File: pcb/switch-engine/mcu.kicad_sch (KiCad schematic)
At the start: 67 parts, among them J10 CORTEX_DEBUG_ETM, J11 CONN_01X03, J12 CONN_01X03, J13 PMOD_HOST, J9 PMOD_HOST, U14 ECS-1612MV-250-CN, U16 ECS-1612MV-250-CN, U17 AT24MAC402, U8 XILINX_ULTRASCALEPLUS_B676, U9 STM32H735-UFBGA176-25

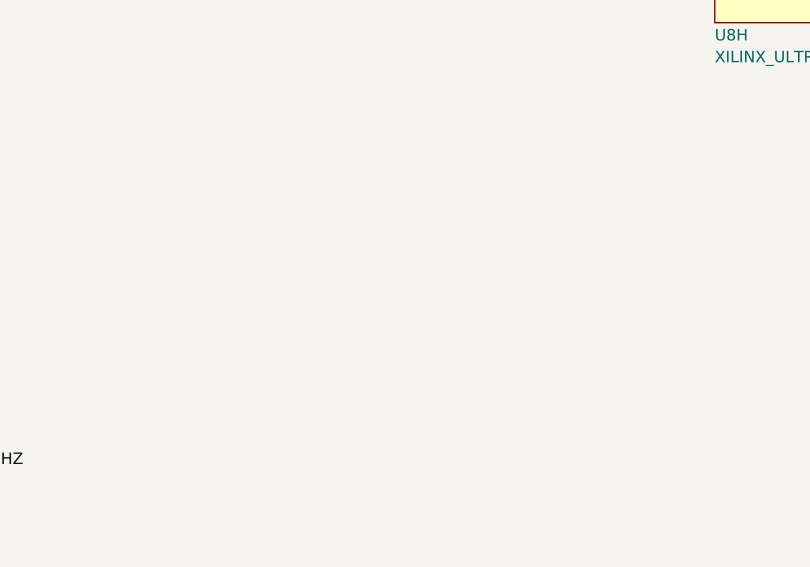
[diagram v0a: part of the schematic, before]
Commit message: Continued initial schematic work on switch engine
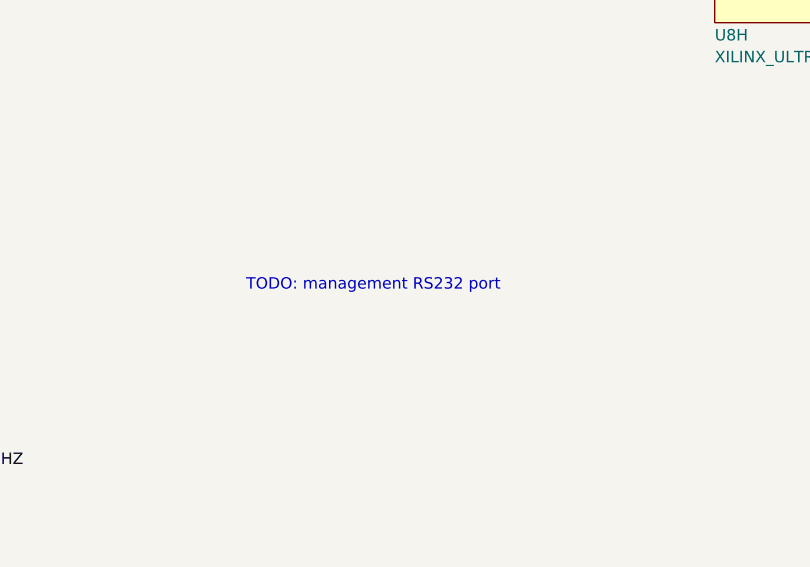
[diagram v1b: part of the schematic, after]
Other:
- note added: "TODO: management RS232 port"
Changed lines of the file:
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@@
+		)
+	)
+	(text "TODO: management RS232 port"
+		(exclude_from_sim no)
+		(at 295.91 214.63 0)
+		(effects
+			(font
+				(size 1.27 1.27)
+			)
+			(justify left)
 		)
 	)

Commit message: First iteration of main board PCB schematic is now passing ERC
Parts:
- removed C102: 0.47 uF, azonenberg_pcb:EIA_0402_CAP_NOSILK, symbol device:C
- removed J11: CONN_01X03, azonenberg_pcb:CONN_HEADER_2.54MM_1x3, symbol conn:CONN_01X03
- removed R71: 33, azonenberg_pcb:EIA_0402_RES_NOSILK, symbol device:R
- removed U16: ECS-1612MV-250-CN, azonenberg_pcb:OSCILLATOR_1.6x1.2, symbol osc-azonenberg:OSC
- added C149: 0.47 uF, azonenberg_pcb:EIA_0402_CAP_NOSILK, symbol device:C
- added C150, C151, C152, C153: 0.1 uF, azonenberg_pcb:EIA_0402_CAP_NOSILK, symbol device:C
- added J24, J25: JUMPER_0402_SPDT, azonenberg_pcb:EIA_0402_JUMPER, symbol special-azonenberg:JUMPER_0402_SPDT
- added J26: RJ45, azonenberg_pcb:CONN_RJ45_BELSTEWART_SS-7188S-A-PG4-1-BA-xx, symbol conn:RJ45
- added TP25, TP26, TP27, TP28: CONN_01X03, azonenberg_pcb:CONN_HEADER_2.54MM_1x3, symbol conn:CONN_01X03
- added U29: ADM3101E_QFN, azonenberg_pcb:QFN_12_0.5MM_3x3MM, symbol special-azonenberg:ADM3101E_QFN
- U8: value XILINX_ULTRASCALEPLUS_B676 -> XCKU5P-2FFVB676I
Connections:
- net FPGA_CLK_25MHZ is gone; now on net FMC_AD4: U8.E13 (IO_L7P_HDGC_87)
- net 3V3: now also C149.1, U29.5 (VCC)
- net GND: now also C149.2, C151.2, C153.2, J26.4, J26.5, J26.9 (SHIELD), TP25.3 (P3), TP26.3 (P3), TP27.3 (P3), TP28.3 (P3), U29.6 (GND), U29.PAD (GND)
- net MCU_UART_RX: now also TP28.1 (P1), U29.2 (Rout)
- net MCU_UART_TX: now also TP28.2 (P2), U29.3 (Tin)
- net MGMT_I2C_SCL: now also TP25.2 (P2)
- net MGMT_I2C_SDA: now also TP25.1 (P1)
- net SFP0_SCL: now also TP26.2 (P2)
- net SFP0_SDA: now also TP26.1 (P1)
- net SFP1_SCL: now also TP27.2 (P2)
- net SFP1_SDA: now also TP27.1 (P1)
- net FAN2_PWM: now reaches U9.N5 (PA3)
- net FAN1_TACH: now reaches U9.P1 (PA0)
- net FAN2_TACH: now reaches U9.P2 (PA1)
- net FAN1_PWM: now reaches U9.R2 (PA2)
- new net: C150.1, U29.11 (C2+)
- new net: C150.2, U29.10 (C2-)
- new net: C153.1, U29.4 (V+)
- new net: C152.1, U29.1 (C1+)
- new net: C152.2, U29.12 (C1-)
- new net: C151.1, U29.7 (V-)
- new net RS232_RX: J24.3, J25.1, U29.9 (Rin)
- new net RS232_RX_RJ45: J25.2, J26.6
- new net RS232_TX: J24.1, J25.3, U29.8 (Tout)
- new net RS232_TX_RJ45: J24.2, J26.3
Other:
- note added: "Clocks"
- note added: "FPGA GPIO"
- note added: "FPGA IOs to MCU"
- note added: "MAC EEPROM"
- note added: "MCU GPIO"
- note added: "MCU IO banks"
- note added: "MCU power/debug"
- note added: "RS232 console"
- note added: "TX/RX crossover jumpers in case we got the RJ45 pinout wrong :)"
- note added: "Test points"
- note removed: "TODO: management RS232 port"
- company: (none) -> Antikernel Labs
- title: (none) -> LATENTRED Ethernet Switch - Main Board
- moved on the sheet: C100, C101, C103, C72, C73, C74, C75, C76, C77, C78, C79, C80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

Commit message: Finished schematic review
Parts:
- removed J24, J25: JUMPER_0402_SPDT, azonenberg_pcb:EIA_0402_JUMPER, symbol special-azonenberg:JUMPER_0402_SPDT
- added R71, R9: 0, symbol device:R
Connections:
- net RS232_RX: now also R71.1
- net RS232_RX_RJ45: now also R71.2
- net RS232_TX: now also R9.1
- net RS232_TX_RJ45: now also R9.2
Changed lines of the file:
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@@
 	(text "TX/RX crossover jumpers\nin case we got the RJ45 pinout wrong :)"
 		(exclude_from_sim no)
-		(at 314.96 193.04 0)
+		(at 307.34 179.07 0)
 		(effects
 			(font
@@
 	)
 	(label "RS232_RX_RJ45"
-		(at 307.34 182.88 180)
+		(at 314.96 172.72 0)
 		(fields_autoplaced yes)
 		(effects
@@
 				(size 1.27 1.27)
 			)
-			(justify right bottom)
+			(justify left bottom)
 		)
 	)
@@
 		)
 	)
-	(label "RS232_TX"
-		(at 307.34 185.42 180)
-		(fields_autoplaced yes)
-		(effects
-			(font
-				(size 1.27 1.27)
-			)
-			(justify right bottom)
-		)
-	)
 	(label "FMC_NOE"
 		(at 228.6 62.23 180)
@@
 		)
 	)
-	(label "RS232_RX"
-		(at 307.34 172.72 180)
-		(fields_autoplaced yes)
-		(effects
-			(font
-				(size 1.27 1.27)
-			)
-			(justify right bottom)
-		)
-	)
 	(label "GND"
 		(at 306.07 106.68 180)
@@
 	)
 	(label "RS232_RX"
-		(at 307.34 180.34 180)
+		(at 307.34 172.72 180)
 		(fields_autoplaced yes)
 		(effects
@@
 	)
 	(label "RS232_TX_RJ45"
-		(at 307.34 170.18 180)
+		(at 314.96 167.64 0)
 		(fields_autoplaced yes)
 		(effects
@@
 				(size 1.27 1.27)
 			)
-			(justify right bottom)
+			(justify left bottom)
 		)
 	)
@@
 	)
 	(symbol
-		(lib_id "special-azonenberg:JUMPER_0402_SPDT")
-		(at 314.96 175.26 0)
-		(mirror y)
-		(unit 1)
-		(exclude_from_sim no)
-		(in_bom yes)
-		(on_board yes)
-		(dnp no)
-		(fields_autoplaced yes)
-		(property "Reference" "J24"
-			(at 324.485 169.1153 0)
-			(effects
-				(font
-					(size 1.524 1.524)
-				)
-				(justify right)
-			)
-		)
-		(property "Value" "JUMPER_0402_SPDT"
-			(at 324.485 172.3943 0)
-			(effects
-				(font
-					(size 1.524 1.524)
-				)
-				(justify right)
-			)
-		)
-		(property "Footprint" "azonenberg_pcb:EIA_0402_JUMPER"
-			(at 314.96 175.26 0)
-			(effects
-				(font
-					(size 1.524 1.524)
-				)
-				(hide yes)
-			)
-		)
-		(property "Datasheet" ""
-			(at 314.96 175.26 0)
-			(effects
-				(font
-					(size 1.524 1.524)
-				)
-			)
-		)
-		(property "Description" ""
-			(at 314.96 175.26 0)
-			(effects
-				(font
-					(size 1.27 1.27)
-				)
-				(hide yes)
-			)
-		)
-		(pin "1"
-		)
-		(pin "2"
-		)
-		(pin "3"
-		)
-		(instances
-			(project "switch-engine"
-				(path "/2594b26d-2fe5-4054-81d2-ca5df3747243/16e4b61f-e96f-427b-b17b-02c8899758b5"
-					(reference "J24")
-					(unit 1)
-				)
-			)
-		)
-	)
-	(symbol
 		(lib_id "device:C")
 		(at 99.06 138.43 0)
@@
 	)
 	(symbol
+		(lib_id "device:R")
+		(at 311.15 172.72 90)
+		(unit 1)
+		(exclude_from_sim no)
+		(in_bom yes)
+		(on_board yes)
+		(dnp no)
+		(property "Reference" "R71"
+			(at 311.15 170.18 90)
+			(effects
+				(font
+					(size 1.27 1.27)
+				)
+			)
+		)
+		(property "Value" "0"
+			(at 311.15 172.72 90)
+			(effects
+				(font
+					(size 1.27 1.27)
+				)
+			)
+		)
+		(property "Footprint" ""
+			(at 311.15 174.498 90)
+			(effects
+				(font
+					(size 1.27 1.27)
+				)
+				(hide yes)
+			)
+		)
+		(property "Datasheet" ""
+			(at 311.15 172.72 0)
+			(effects
+				(font
+					(size 1.27 1.27)
+				)
+				(hide yes)
+			)
+		)
+		(property "Description" "Resistor"
+			(at 311.15 172.72 0)
+			(effects
+				(font
+					(size 1.27 1.27)
+				)
+				(hide yes)
+			)
+		)
+		(pin "2"
+		)
+		(pin "1"
+		)
+		(instances
+			(project "switch-engine"
+				(path "/2594b26d-2fe5-4054-81d2-ca5df3747243/16e4b61f-e96f-427b-b17b-02c8899758b5"
+					(reference "R71")
+					(unit 1)
+				)
+			)
+		)
+	)
+	(symbol
 		(lib_id "st-azonenberg:STM32H735-UFBGA176-25")
 		(at 182.88 115.57 0)
@@
 	)
 	(symbol
-		(lib_id "special-azonenberg:JUMPER_0402_SPDT")
-		(at 314.96 187.96 0)
-		(mirror y)
-		(unit 1)
-		(exclude_from_sim no)
-		(in_bom yes)
-		(on_board yes)
-		(dnp no)
-		(fields_autoplaced yes)
-		(property "Reference" "J25"
-			(at 324.485 181.8153 0)
-			(effects
-				(font
-					(size 1.524 1.524)
-				)
-				(justify right)
-			)
-		)
-		(property "Value" "JUMPER_0402_SPDT"
-			(at 324.485 185.0943 0)
-			(effects
-				(font
-					(size 1.524 1.524)
-				)
-				(justify right)
-			)
-		)
-		(property "Footprint" "azonenberg_pcb:EIA_0402_JUMPER"
-			(at 314.96 187.96 0)
-			(effects
-				(font
-					(size 1.524 1.524)
-				)
-				(hide yes)
-			)
-		)
-		(property "Datasheet" ""
-			(at 314.96 187.96 0)
-			(effects
-				(font
-					(size 1.524 1.524)
-				)
-			)
-		)
-		(property "Description" ""
-			(at 314.96 187.96 0)
-			(effects
-				(font
-					(size 1.27 1.27)
-				)
-				(hide yes)
-			)
-		)
-		(pin "1"
-		)
-		(pin "2"
-		)
-		(pin "3"
-		)
-		(instances
-			(project "switch-engine"
-				(path "/2594b26d-2fe5-4054-81d2-ca5df3747243/16e4b61f-e96f-427b-b17b-02c8899758b5"
-					(reference "J25")
-					(unit 1)
-				)
-			)
-		)
-	)
-	(symbol
 		(lib_id "conn:CONN_01X03")
 		(at 233.68 218.44 0)
@@
 				)
 			)
+		)
+	)
+	(symbol
+		(lib_id "device:R")
+		(at 311.15 167.64 90)
+		(unit 1)
+		(exclude_from_sim no)
+		(in_bom yes)
+		(on_board yes)
+		(dnp no)
+		(property "Reference" "R9"
+			(at 311.15 165.1 90)
+			(effects
+				(font
+					(size 1.27 1.27)
+				)
+			)
+		)
+		(property "Value" "0"
+			(at 311.15 167.64 90)
+			(effects
+				(font
+					(size 1.27 1.27)
+				)
+			)
+		)
+		(property "Footprint" ""
+			(at 311.15 169.418 90)
+			(effects
+				(font
+					(size 1.27 1.27)
+				)
+				(hide yes)
+			)
+		)
+		(property "Datasheet" ""
+			(at 311.15 167.64 0)
+			(effects
+				(font
+					(size 1.27 1.27)
+				)
+				(hide yes)
+			)
+		)
+		(property "Description" "Resistor"
+			(at 311.15 167.64 0)
+			(effects
+				(font
+					(size 1.27 1.27)
+				)
+				(hide yes)
+			)
+		)
+		(pin "2"
+		)
+		(pin "1"
+		)
+		(instances
+			(project ""
+				(path "/2594b26d-2fe5-4054-81d2-ca5df3747243/16e4b61f-e96f-427b-b17b-02c8899758b5"
+					(reference "R9")
+					(unit 1)
+				)
+			)

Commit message: Added footprints and created initial skeleton of layout
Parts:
- R71, R9: footprint (none) -> azonenberg_pcb:EIA_0402_RES_NOSILK
- U8: footprint (none) -> azonenberg_pcb:BGA_676_27x27_FULLARRAY_1MM_FFG676
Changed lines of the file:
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@@
 			)
 		)
-		(property "Footprint" ""
+		(property "Footprint" "azonenberg_pcb:EIA_0402_RES_NOSILK"
 			(at 311.15 174.498 90)
 			(effects
@@
 			)
 		)
-		(property "Footprint" ""
+		(property "Footprint" "azonenberg_pcb:EIA_0402_RES_NOSILK"
 			(at 311.15 169.418 90)
 			(effects
@@
 			)
 		)
-		(property "Footprint" ""
+		(property "Footprint" "azonenberg_pcb:BGA_676_27x27_FULLARRAY_1MM_FFG676"
 			(at 297.18 80.01 0)
 			(effects
@@
 			)
 		)
-		(property "Footprint" ""
+		(property "Footprint" "azonenberg_pcb:BGA_676_27x27_FULLARRAY_1MM_FFG676"
 			(at 363.22 80.01 0)
 			(effects

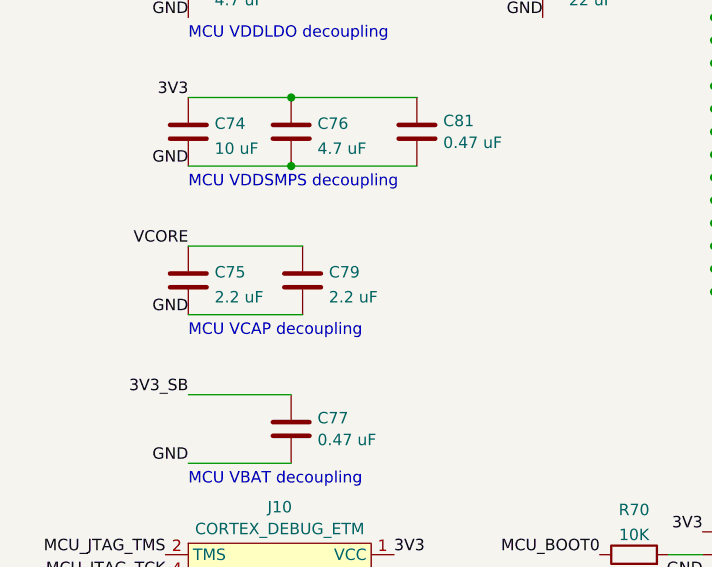
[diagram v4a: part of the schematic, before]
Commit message: Initial rough floorplan
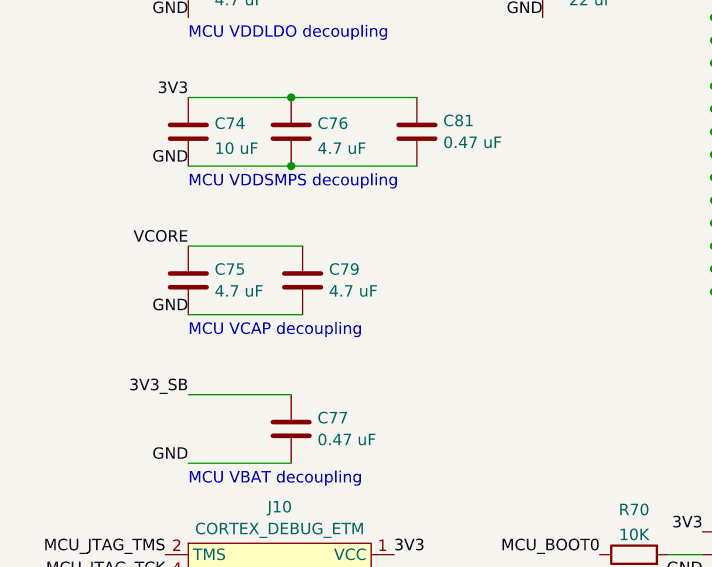
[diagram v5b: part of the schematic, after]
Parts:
- C75, C79: value 2.2 uF -> 4.7 uF; footprint azonenberg_pcb:EIA_0805_CAP_NOSILK -> azonenberg_pcb:EIA_0603_CAP_NOSILK
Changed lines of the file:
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@@
 		(fields_autoplaced yes)
 		(property "Reference" "C79"
-			(at 46.101 204.8315 0)
+			(at 46.101 204.5278 0)
 			(effects
 				(font
@@
 			)
 		)
-		(property "Value" "2.2 uF"
-			(at 46.101 207.6066 0)
+		(property "Value" "4.7 uF"
+			(at 46.101 206.9521 0)
 			(effects
 				(font
@@
 			)
 		)
-		(property "Footprint" "azonenberg_pcb:EIA_0805_CAP_NOSILK"
+		(property "Footprint" "azonenberg_pcb:EIA_0603_CAP_NOSILK"
 			(at 44.1452 209.55 0)
 			(effects
@@
 		(fields_autoplaced yes)
 		(property "Reference" "C75"
-			(at 33.401 204.8315 0)
+			(at 33.401 204.5278 0)
 			(effects
 				(font
@@
 			)
 		)
-		(property "Value" "2.2 uF"
-			(at 33.401 207.6066 0)
+		(property "Value" "4.7 uF"
+			(at 33.401 206.9521 0)
 			(effects
 				(font
@@
 			)
 		)
-		(property "Footprint" "azonenberg_pcb:EIA_0805_CAP_NOSILK"
+		(property "Footprint" "azonenberg_pcb:EIA_0603_CAP_NOSILK"
 			(at 31.4452 209.55 0)
 			(effects
